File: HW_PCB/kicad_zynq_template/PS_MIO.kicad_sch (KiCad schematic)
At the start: 27 parts, among them U1 SiT8008AI-73-XXS-33.333333E, U2 XA7Z020-1CLG400I, U3 W25Q256FVBIG, U4 W25Q256FVBIG

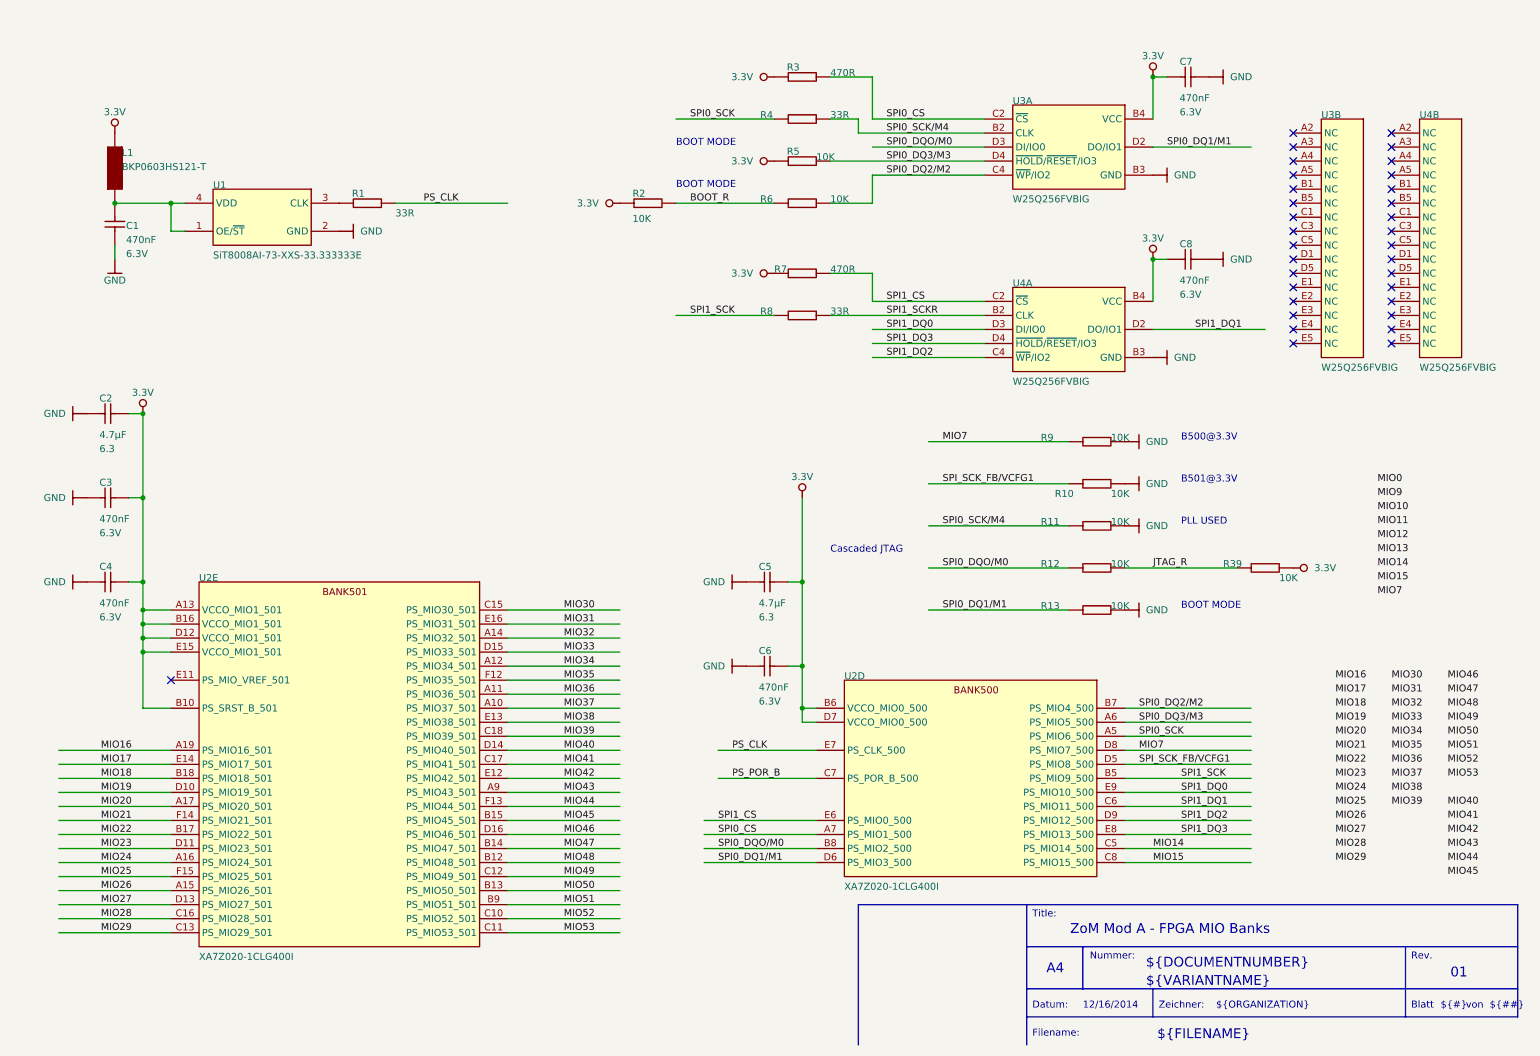
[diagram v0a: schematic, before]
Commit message: pcbs tidied up
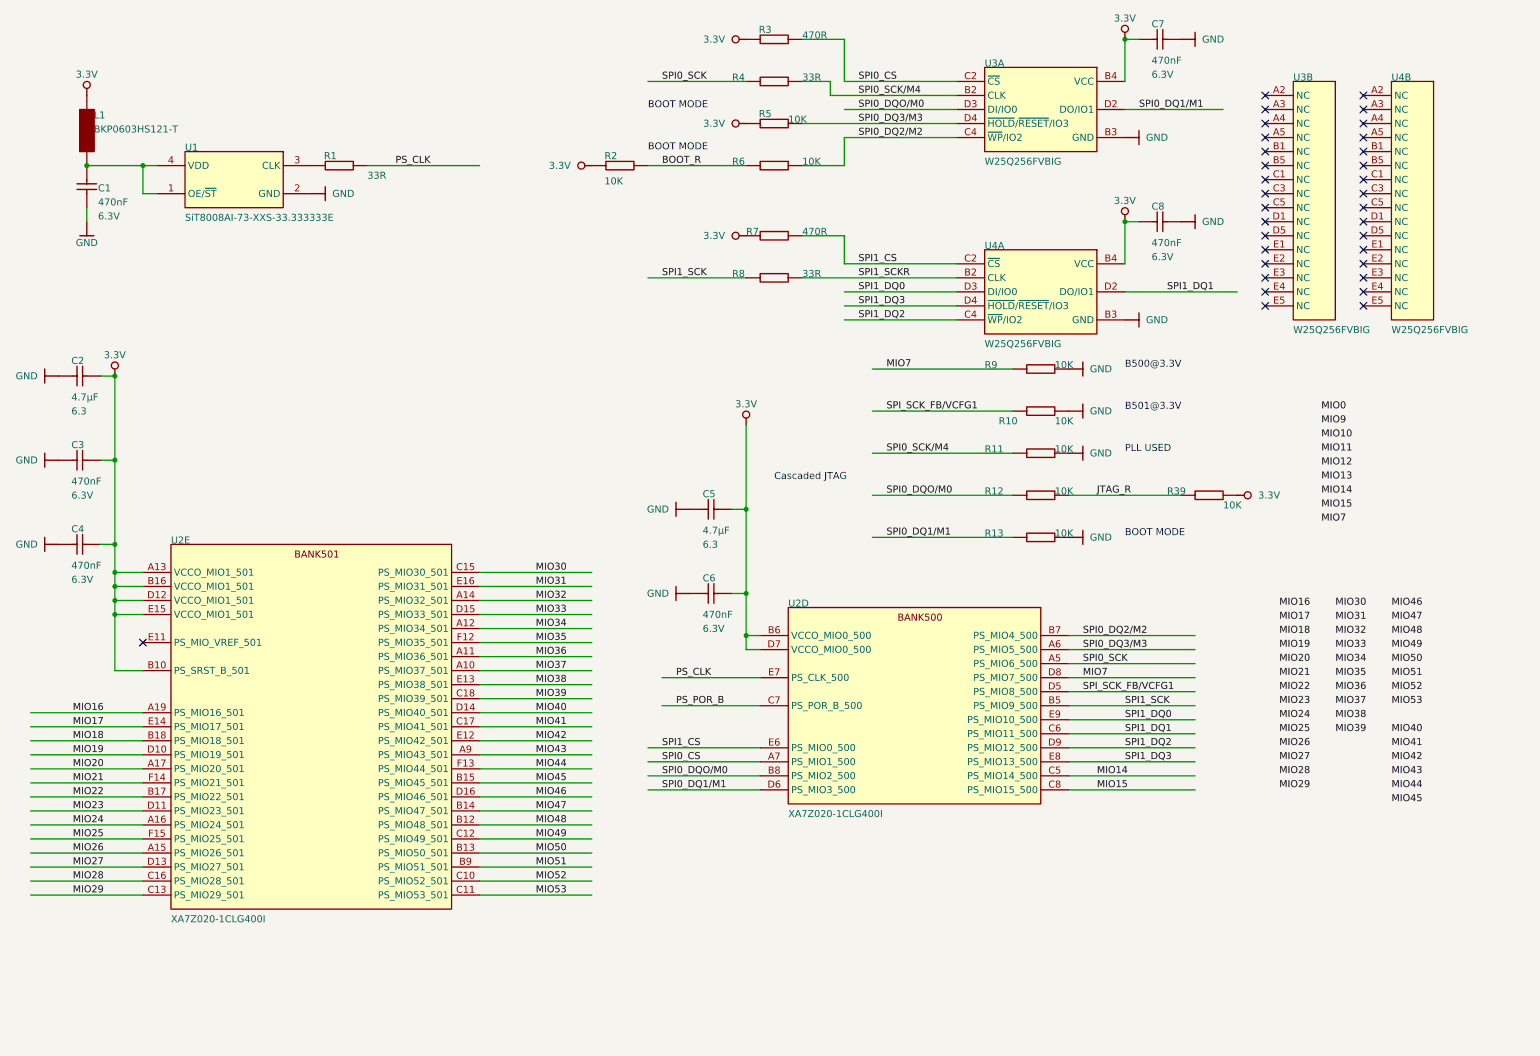
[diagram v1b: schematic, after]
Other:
- note removed: "${##}"
- note removed: "${#}"
- note removed: "${DOCUMENTNUMBER}"
- note removed: "${FILENAME}"
- note removed: "${ISSUE_DATE}"
- note removed: "${ORGANIZATION}"
- note removed: "${REVISION}"
- note removed: "${TITLE}"
- note removed: "${VARIANTNAME}"
- note removed: "A4"
- note removed: "Blatt"
- note removed: "Datum:"
- note removed: "Filename:"
- note removed: "Nummer:"
- note removed: "Rev."
- note removed: "Title:"
- note removed: "Zeichner:"
- note removed: "von"
- moved on the sheet: C1, C2, C3, C4, C5, C6, C7, C8, L1, R1, R10, R11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
